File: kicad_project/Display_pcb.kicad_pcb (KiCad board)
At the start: 4 copper layers, 60.6 x 27.6 mm, 87 parts, among them IC1 ESP32-S3R8, J1 Micro_SD_Card_Det_Hirose_DM3AT, J2 USB C, J8 33FXRH-SM1-GAN-TF, SW1 B3U-1000P, SW2 B3U-1000P, SW3 B3U-1000P, U1 W25Q128JVSIQ, U2 SY8089A1AAC, U4 SY8089A1AAC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

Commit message: Design revision: SD improvements, flash update, silkscreen and USB differential fix
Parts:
- removed R8: TBD, Resistor_SMD:R_0402_1005Metric
- added G***: LOGO, smd-non-ipc:QR_webscreenCC, F.Cu at (160.4, 92.6)
- added R20: 10k, Resistor_SMD:R_0402_1005Metric, F.Cu at (164.8, 99.1)
- added REF**: CE-Logo_8.5x6mm_SilkScreen, Symbol:CE-Logo_8.5x6mm_SilkScreen, B.Cu at (131.5, 90.4)
- added REF**: WEEE-Logo_4.2x6mm_SilkScreen, Symbol:WEEE-Logo_4.2x6mm_SilkScreen, B.Cu at (167.9, 90.4)
- added REF**: OSHW-Logo_5.7x6mm_SilkScreen, Symbol:OSHW-Logo_5.7x6mm_SilkScreen, B.Cu at (174.2, 90.4)
- G***: moved to B.Cu
- moved G*** 30.0 mm to (131.7, 95.9), turned to 0 degrees
- moved C13 3.46 mm to (164.4, 100.8)
- moved C15 1.55 mm to (135.9, 106.3), turned to 0 degrees
- moved C19 1.20 mm to (128.1, 99.9), turned to 90 degrees
- moved G*** 0.95 mm to (162.7, 110.0)
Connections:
- net /MCU/USB_N renamed /USB-
- net /USB_P renamed /USB+
- IC1 pad 15: /GPIO10 -> /CS
- IC1 pad 28: /Flash_Memory/SPICS1 -> /MCU/SPICS1
- J1 pad 2: /microSdCard/CS_SD -> /CS
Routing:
- net /CS: track 0.00 -> 51.4 mm, vias 0 -> 2
- net /USB+: track 14.5 -> 19.1 mm
- net VDD_SPI: track 50.6 -> 47.5 mm, vias 3 -> 4
- net /OL_SD0: track 42.7 -> 39.6 mm
- net /DAT0: track 48.5 -> 45.9 mm
- net /Flash_Memory/SPICS1: track 2.43 -> 0.00 mm, vias 1 -> 0
- net GND: track 127.3 -> 125.1 mm, vias 334 -> 333
- net /Flash_Memory/SPICS0: track 18.9 -> 17.2 mm
- net /OL_D1: track 41.9 -> 43.6 mm
- net /USB-: track 17.8 -> 19.2 mm
- net /OL_TE: track 44.7 -> 43.4 mm
- net /CMD: track 48.6 -> 47.4 mm, vias 2 -> 3
- net /POWER/VBUS: track 51.4 -> 50.6 mm
- net /Flash_Memory/SPIWP: track 20.9 -> 20.2 mm
- net /OL_SCK: track 27.7 -> 27.1 mm
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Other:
- board text added: "webscreen.cc"
- board text removed: "WebScreen PCB"

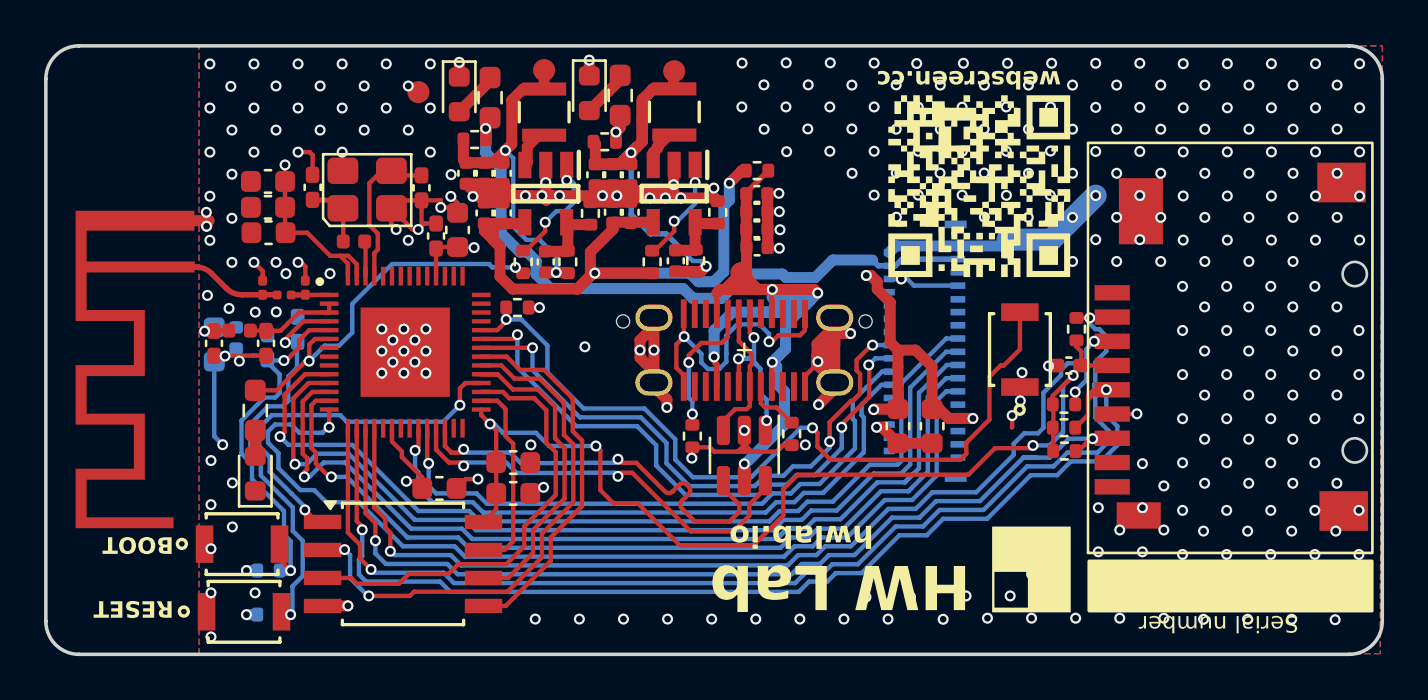
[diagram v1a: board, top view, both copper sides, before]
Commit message: Change SD card power source from VDD_SPI to 3V3 to support A1 cards
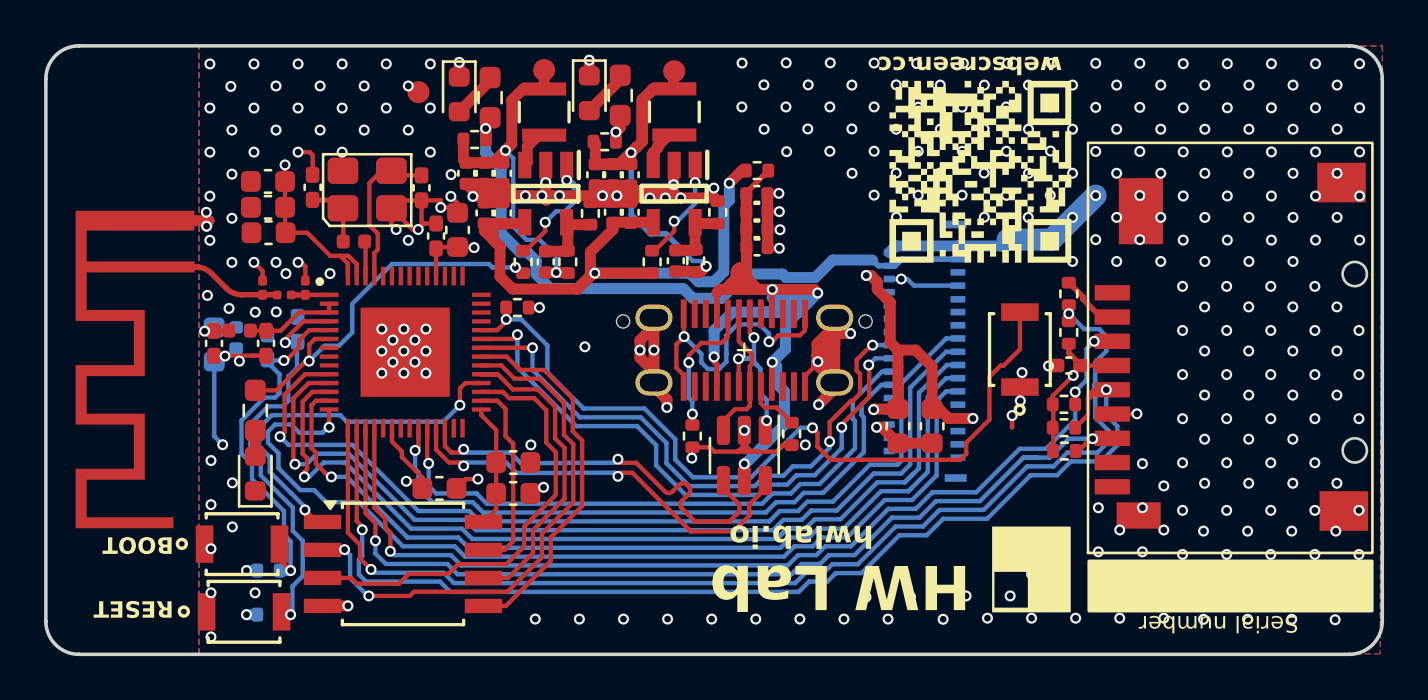
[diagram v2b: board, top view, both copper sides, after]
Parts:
- added R8: 0R, Resistor_SMD:R_0402_1005Metric, F.Cu at (164.4, 97.5)
- moved G*** 0.65 mm to (160.4, 92.0)
- moved R20 0.38 mm to (164.4, 99.2)
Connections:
- C13 pad 1: VDD_SPI -> +3V3
- J1 pad 2: /CS -> Net-(J1-DAT3/CD)
- J1 pad 4: VDD_SPI -> +3V3
- R12 pad 1: VDD_SPI -> +3V3
- R20 pad 1: VDD_SPI -> +3V3
- R3 pad 1: VDD_SPI -> +3V3
- R4 pad 1: VDD_SPI -> +3V3
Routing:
- net VDD_SPI: track 47.5 -> 5.62 mm, vias 4 -> 0
- net +3V3: track 29.3 -> 36.2 mm, vias 9 -> 10
- net Net-(J1-DAT3/CD): track 0.00 -> 2.68 mm
- net /CMD: track 47.4 -> 45.7 mm

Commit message: Change logos PcbWay and UK-CA-CE certification
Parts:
- removed the REF** at (131.5, 90.4)
- added G***: LOGO, smd-non-ipc:uk-ca-CE_logo, B.Cu at (131.6, 89.7)
- added G***: LOGO, smd-non-ipc:pcbway_logo, B.Cu at (170.7, 110.5)
- moved G*** 1.85 mm to (131.7, 94.0)
